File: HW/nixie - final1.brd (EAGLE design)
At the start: 160 x 92.4 mm, 17 parts, among them IC1 74141N, IC2 74141N, IC3 74141N, IC4 74141N, IC7 74HC595N, IC8 74HC595N

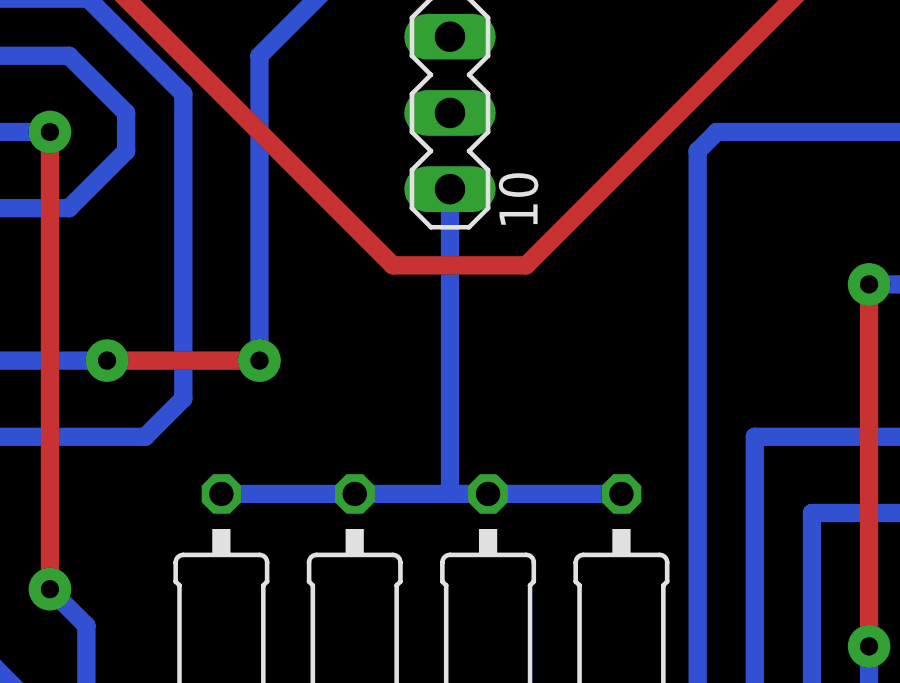
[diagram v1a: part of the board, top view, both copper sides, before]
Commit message: Update HW, SW - hlavne SW blizke HW, hodiny funkcni, bezi testovaci sekvence, na zmacknuti tlacitka se zobrazi
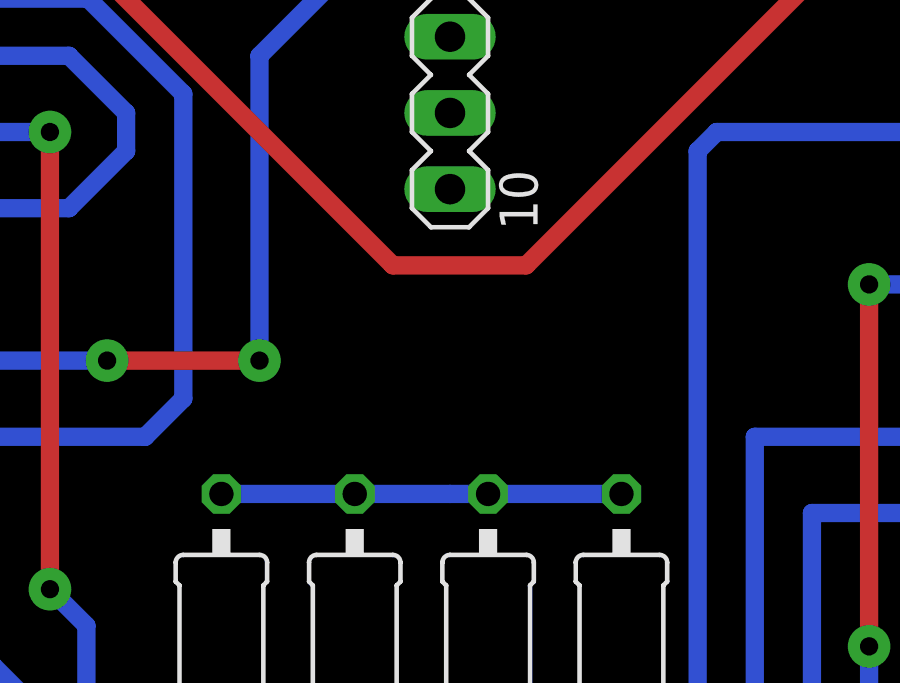
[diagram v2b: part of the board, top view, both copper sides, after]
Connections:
- net 230V= renamed N$41
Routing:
- net N$41: track 23.5 -> 13.3 mm
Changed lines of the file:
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@@
 <?xml version="1.0" encoding="utf-8"?>
 <!DOCTYPE eagle SYSTEM "eagle.dtd">
-<eagle version="9.3.2">
+<eagle version="9.4.0">
 <drawing>
 <settings>
@@
 <contactref element="IC7" pad="8"/>
 <contactref element="IC8" pad="8"/>
-<contactref element="IC1" pad="12"/>
 <contactref element="IC2" pad="12"/>
 <contactref element="IC3" pad="12"/>
@@
 <vertex x="0" y="0"/>
 </polygon>
+<contactref element="IC1" pad="12"/>
 </signal>
 <signal name="VCC">
@@
 <wire x1="79.375" y1="82.55" x2="55.245" y2="82.55" width="0.6096" layer="1"/>
 </signal>
-<signal name="230V=">
-<contactref element="R1" pad="2"/>
-<contactref element="R2" pad="2"/>
-<contactref element="R3" pad="2"/>
-<contactref element="R4" pad="2"/>
-<contactref element="SV1" pad="10"/>
-<wire x1="79.375" y1="59.69" x2="79.375" y2="49.53" width="0.6096" layer="16"/>
-<wire x1="79.375" y1="49.53" x2="76.2" y2="49.53" width="0.6096" layer="16"/>
-<wire x1="76.2" y1="49.53" x2="71.755" y2="49.53" width="0.6096" layer="16"/>
-<wire x1="79.375" y1="49.53" x2="80.645" y2="49.53" width="0.6096" layer="16"/>
-<wire x1="80.645" y1="49.53" x2="85.09" y2="49.53" width="0.6096" layer="16"/>
-</signal>
 <signal name="N$89">
 <contactref element="R1" pad="1"/>
@@
 <wire x1="107.315" y1="36.195" x2="139.7" y2="36.195" width="0.6096" layer="1"/>
 </signal>
+<signal name="N$41">
+<contactref element="SV1" pad="10"/>
+<contactref element="R1" pad="2"/>
+<contactref element="R2" pad="2"/>
+<contactref element="R3" pad="2"/>
+<contactref element="R4" pad="2"/>
+<wire x1="79.375" y1="49.53" x2="76.2" y2="49.53" width="0.6096" layer="16"/>
+<wire x1="76.2" y1="49.53" x2="71.755" y2="49.53" width="0.6096" layer="16"/>
+<wire x1="79.375" y1="49.53" x2="80.645" y2="49.53" width="0.6096" layer="16"/>
+<wire x1="80.645" y1="49.53" x2="85.09" y2="49.53" width="0.6096" layer="16"/>
+<wire x1="79.375" y1="49.53" x2="79.375" y2="59.69" width="0" layer="19" extent="16-16"/>
+</signal>
 </signals>
